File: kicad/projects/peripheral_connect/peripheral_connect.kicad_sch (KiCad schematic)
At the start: 63 parts, among them J1 peripheral_addr_bus_connector, J2 peripheral_aux_connector, J3 peripheral_membank_connector, J4 Conn_01x03_Pin, J6 Conn_02x16_Odd_Even, J7 ADDR, J8 DATA, U1 74HC138, U2 74HC138, U3 74HC238, U4 74HC245, U5 74HC238, U6 74HC245, U7 74HC245, U8 74HC245

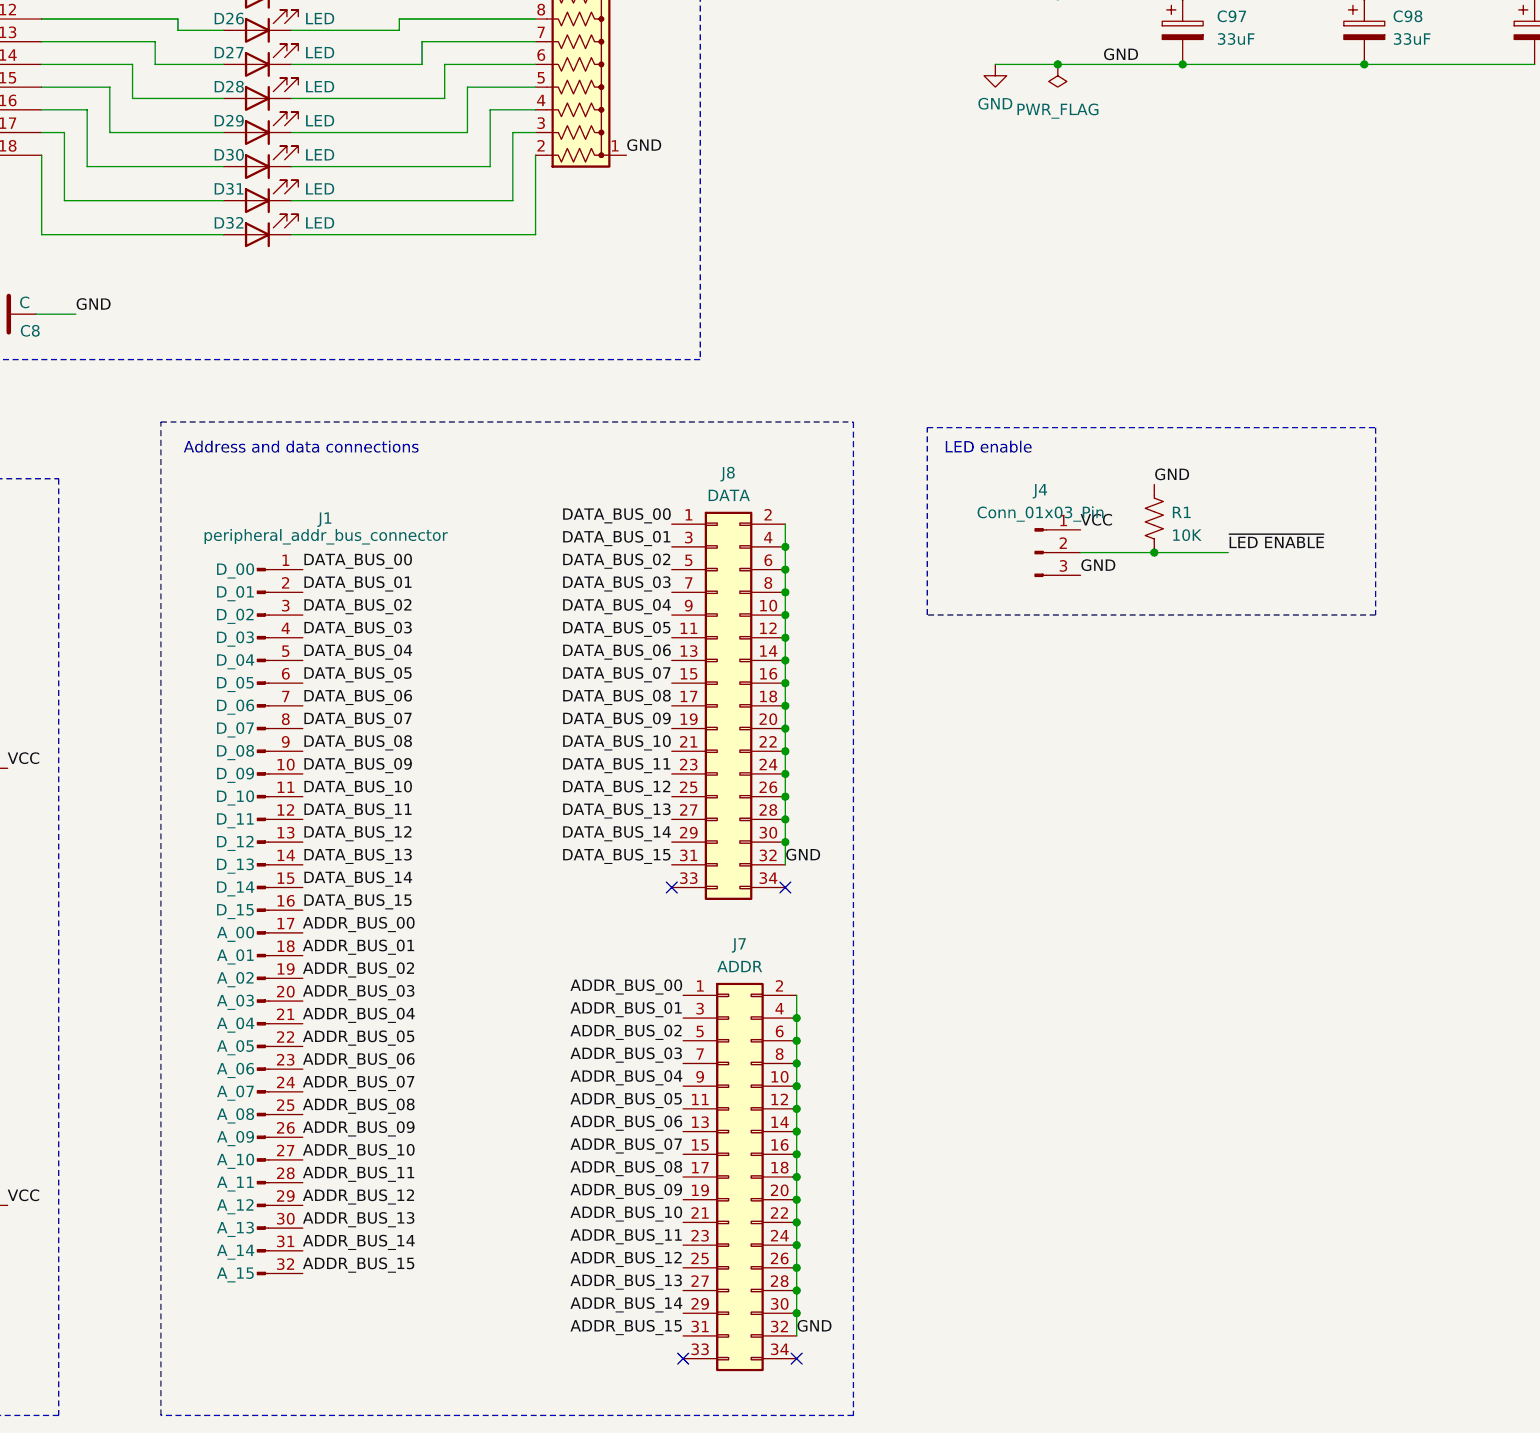
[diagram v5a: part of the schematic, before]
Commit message: Peripheral connect updated to support new bus connect.
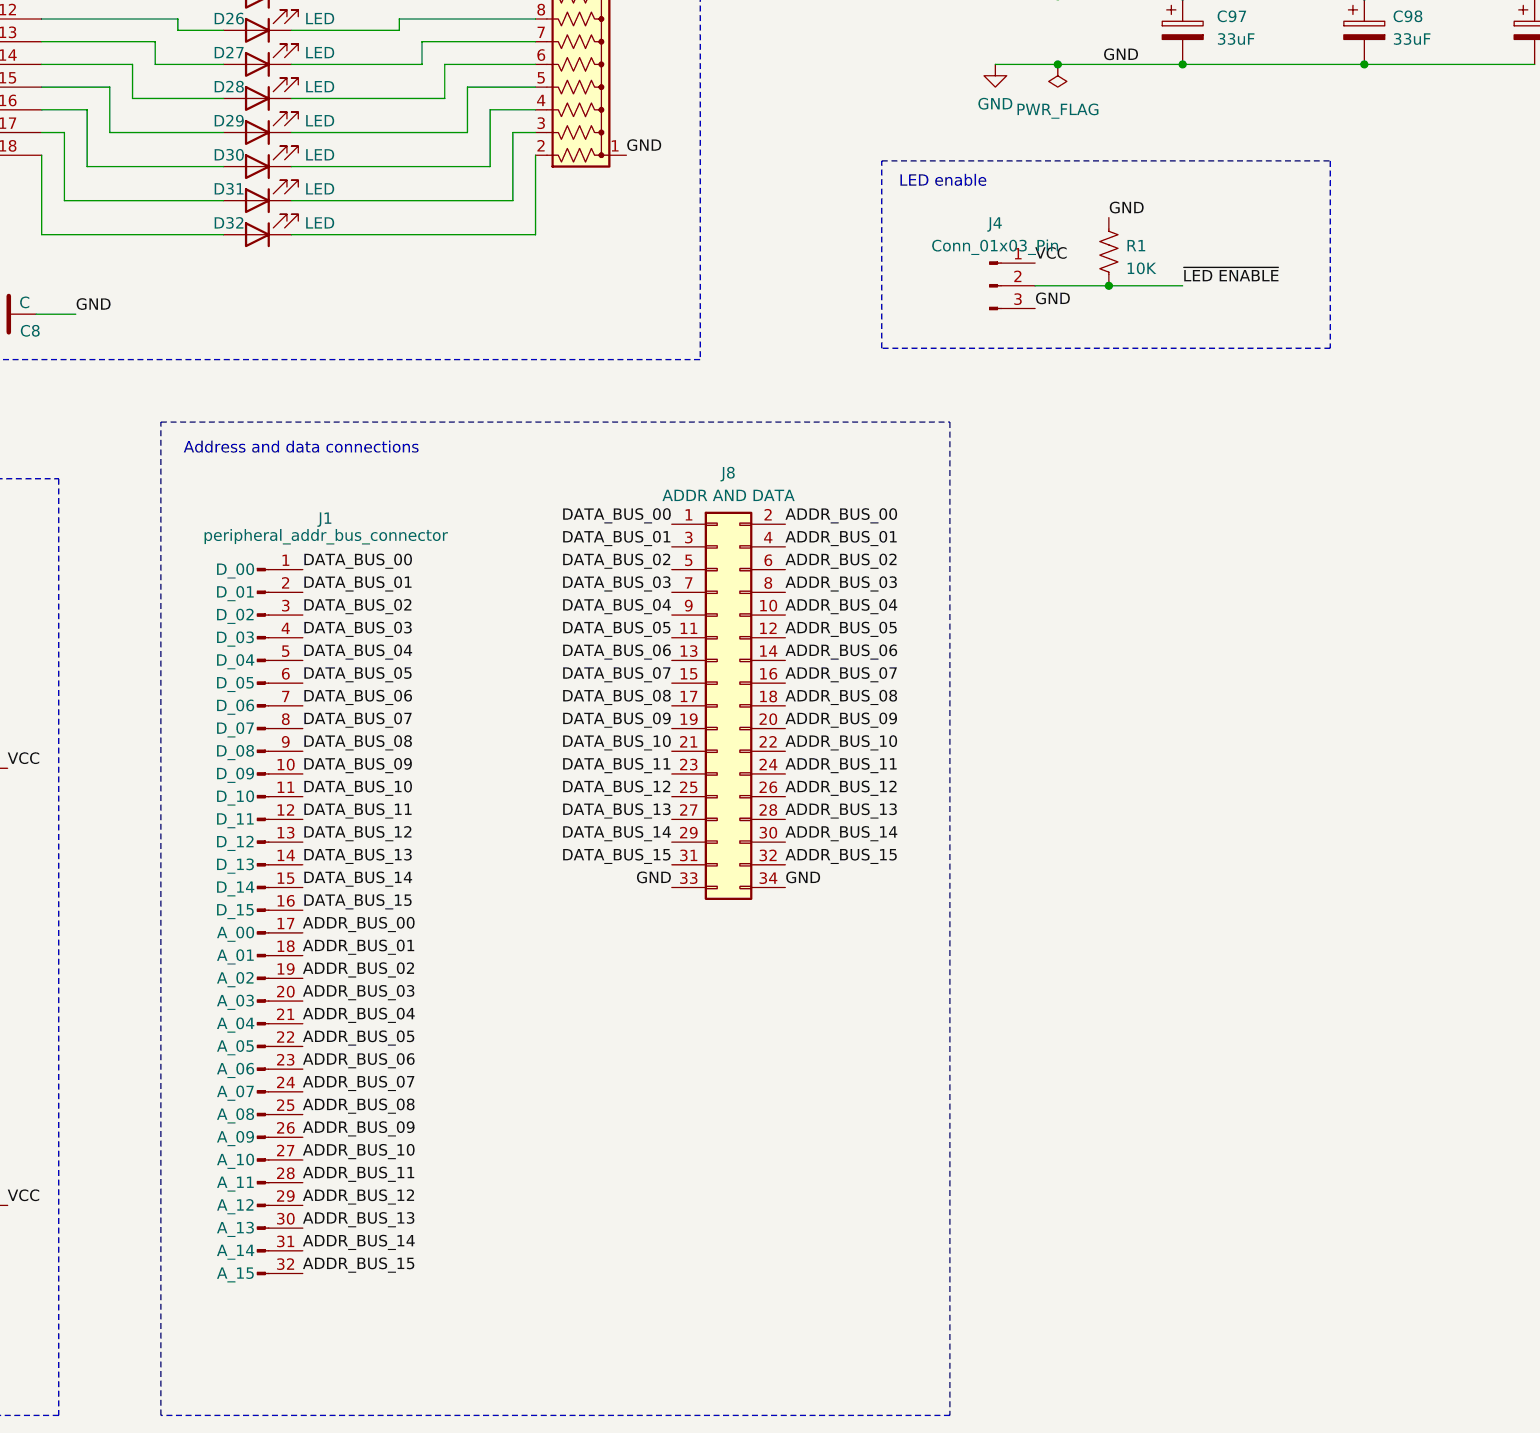
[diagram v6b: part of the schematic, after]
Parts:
- removed J7: ADDR, Connector_PinHeader_2.54mm:PinHeader_2x17_P2.54mm_Vertical, symbol Connector_Generic:Conn_02x17_Odd_Even
- J8: value DATA -> ADDR AND DATA; footprint Connector_PinHeader_2.54mm:PinHeader_2x17_P2.54mm_Vertical -> Connector_PinSocket_2.54mm:PinSocket_2x17_P2.54mm_Horizontal
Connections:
- net ADDR_BUS_00: now also J8.2 (Pin_2)
- net ADDR_BUS_01: now also J8.4 (Pin_4)
- net ADDR_BUS_02: now also J8.6 (Pin_6)
- net ADDR_BUS_03: now also J8.8 (Pin_8)
- net ADDR_BUS_04: now also J8.10 (Pin_10)
- net ADDR_BUS_05: now also J8.12 (Pin_12)
- net ADDR_BUS_06: now also J8.14 (Pin_14)
- net ADDR_BUS_07: now also J8.16 (Pin_16)
- net ADDR_BUS_08: now also J8.18 (Pin_18)
- net ADDR_BUS_09: now also J8.20 (Pin_20)
- net ADDR_BUS_10: now also J8.22 (Pin_22)
- net ADDR_BUS_11: now also J8.24 (Pin_24)
- net ADDR_BUS_12: now also J8.26 (Pin_26)
- net ADDR_BUS_13: now also J8.28 (Pin_28)
- net ADDR_BUS_14: now also J8.30 (Pin_30)
- net ADDR_BUS_15: now also J8.32 (Pin_32)
- net GND: now also J8.33 (Pin_33), J8.34 (Pin_34); no longer J8.10 (Pin_10), J8.12 (Pin_12), J8.14 (Pin_14), J8.16 (Pin_16), J8.18 (Pin_18), J8.2 (Pin_2), J8.20 (Pin_20), J8.22 (Pin_22), J8.24 (Pin_24), J8.26 (Pin_26), J8.28 (Pin_28), J8.30 (Pin_30), J8.32 (Pin_32), J8.4 (Pin_4), J8.6 (Pin_6), J8.8 (Pin_8)
- no-connect marks 9 -> 5
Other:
- moved on the sheet: J4, R1

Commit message: RAM tech checks complete.
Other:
- note added: "Bank Bus is active low"
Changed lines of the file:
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@@
 (kicad_sch (version 20230121) (generator eeschema)
   (paper "B")
-  (bus_alias "BANK_BUS" (members "BANK_BUS_00" "BANK_BUS_01" "BANK_BUS_02" "BANK_BUS_03" "BANK_BUS_04" "BANK_BUS_05" "BANK_BUS_06" "BANK_BUS_07" "BANK_BUS_08" "BANK_BUS_09" "BANK_BUS_10" "BANK_BUS_11" "BANK_BUS_12" "BANK_BUS_13" "BANK_BUS_14" "BANK_BUS_15"))
   (bus_alias "DATA_BUS" (members "DATA_BUS_00" "DATA_BUS_01" "DATA_BUS_02" "DATA_BUS_03" "DATA_BUS_04" "DATA_BUS_05" "DATA_BUS_06" "DATA_BUS_07" "DATA_BUS_08" "DATA_BUS_09" "DATA_BUS_10" "DATA_BUS_11" "DATA_BUS_12" "DATA_BUS_13" "DATA_BUS_14" "DATA_BUS_15"))
   (bus_alias "ADDR_BUS" (members "ADDR_BUS_00" "ADDR_BUS_01" "ADDR_BUS_02" "ADDR_BUS_03" "ADDR_BUS_04" "ADDR_BUS_05" "ADDR_BUS_06" "ADDR_BUS_07" "ADDR_BUS_08" "ADDR_BUS_09" "ADDR_BUS_10" "ADDR_BUS_11" "ADDR_BUS_12" "ADDR_BUS_13" "ADDR_BUS_14" "ADDR_BUS_15"))
+  (bus_alias "BANK_BUS" (members "BANK_BUS_00" "BANK_BUS_01" "BANK_BUS_02" "BANK_BUS_03" "BANK_BUS_04" "BANK_BUS_05" "BANK_BUS_06" "BANK_BUS_07" "BANK_BUS_08" "BANK_BUS_09" "BANK_BUS_10" "BANK_BUS_11" "BANK_BUS_12" "BANK_BUS_13" "BANK_BUS_14" "BANK_BUS_15"))
   (junction (at 106.045 193.675) (diameter 0) (color 0 0 0 0)
   )
@@
     (effects (font (size 1.27 1.27)) (justify left bottom))
   )
+  (text "Bank Bus is active low" (at 289.56 68.58 0)
+    (effects (font (size 1.27 1.27)) (justify left bottom))
+  )
